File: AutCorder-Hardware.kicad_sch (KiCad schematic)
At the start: 61 parts, among them J1 Battery, J2 OV2640, J3 EXT LED, J4 Shutter, J5 Util, J6 Feedback, J7 Micro SD, J8 PWR_ALT, P1 USB_C_Receptacle_USB2.0_16P, Q1 DMP2045U, Q2 DMP2045U, Q3 DMN2040U, SW1 FW, SW2 RESET, U1 ESP32-S3-WROOM-1, U2 MCP73831-2-OT, U3 XC6220B331MR, U4 XC6206P282MR, U5 XC6206P122MR, U6 IMP34DT05TR

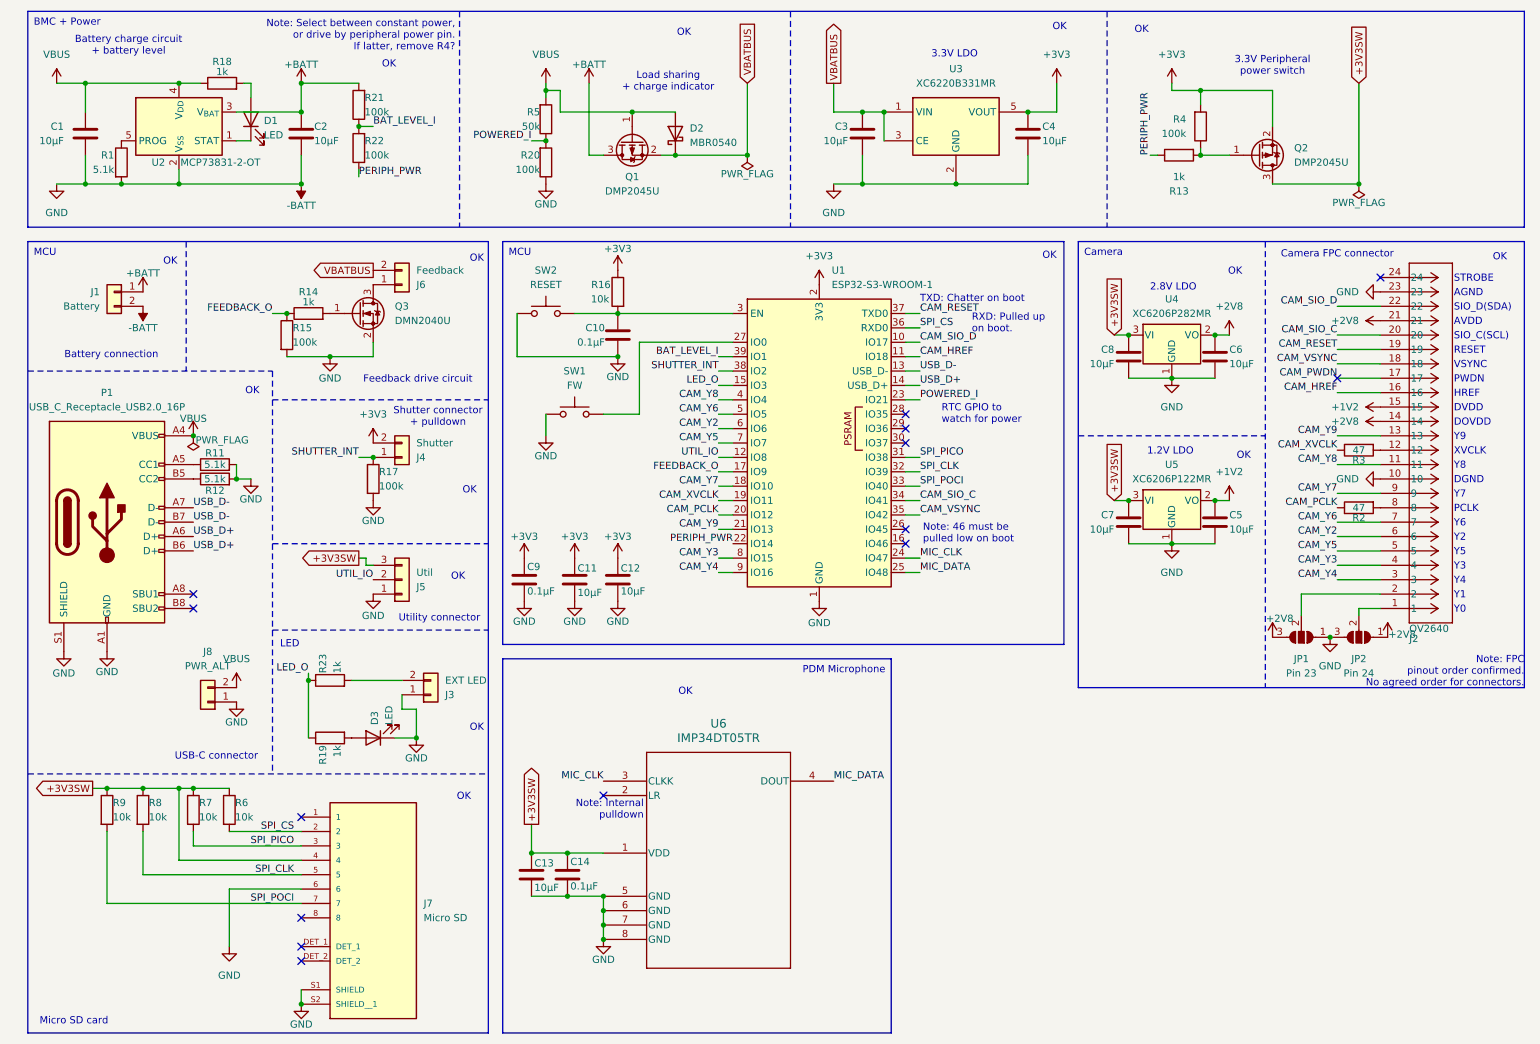
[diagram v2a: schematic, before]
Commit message: Added interactive BOM. Updated KiCad.
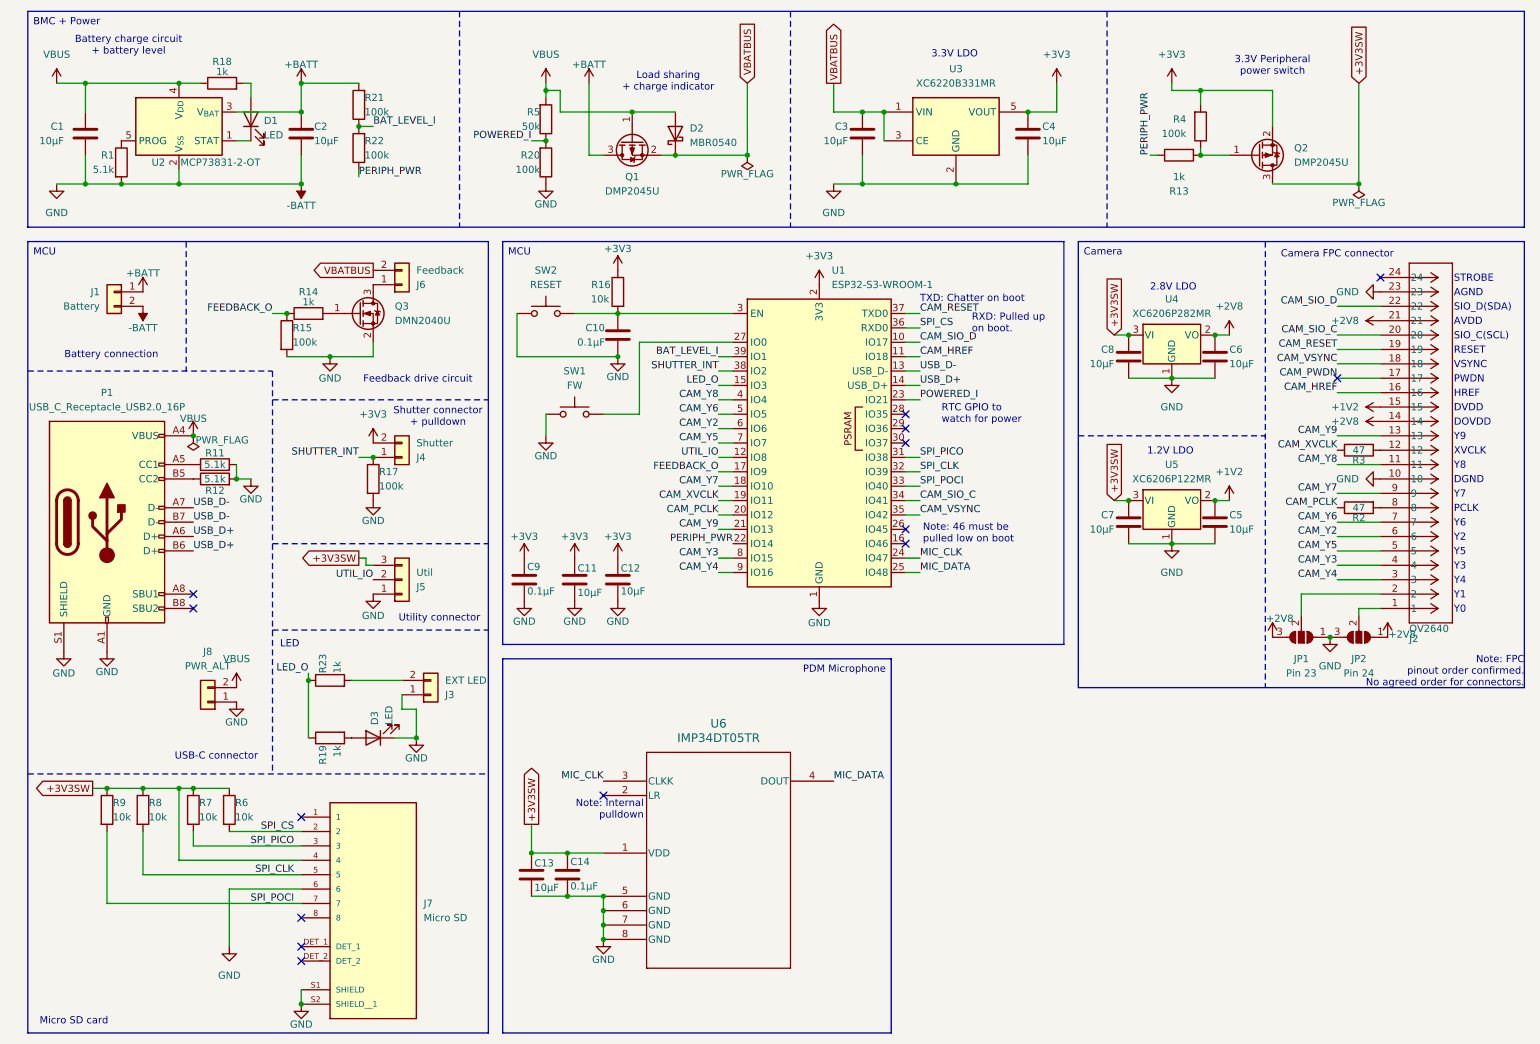
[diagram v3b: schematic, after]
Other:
- note removed: "Note: Select between constant power, or drive by peripheral power pin. If latter, remove R4?"
- note removed: "OK"
